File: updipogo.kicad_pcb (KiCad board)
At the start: 2 copper layers, 32 x 10.7 mm, 13 parts, among them J1 USB_C_Receptacle_USB2.0, J2 1.27, J3 2.54, J4 Header, U1 CH340N

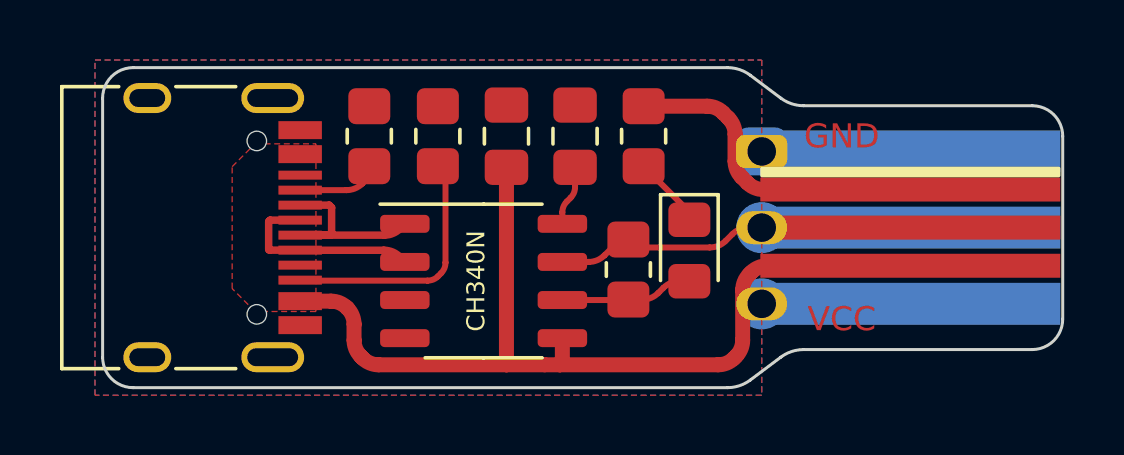
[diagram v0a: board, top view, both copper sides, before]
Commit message: update pcb for new pinout
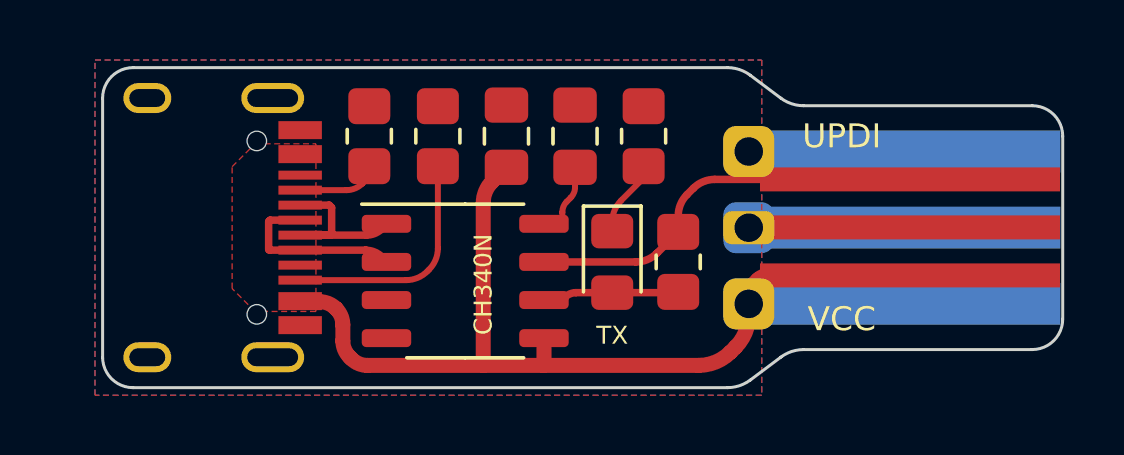
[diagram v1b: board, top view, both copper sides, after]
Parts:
- J2: value 1.27 -> 1.6mm; footprint local:PogoPins_1.27mm -> local:PogoPins_1.6mm
- J3: value 2.54 -> 2.54mm
- moved D1 2.60 mm to (125.7, 77.8)
- moved R3 1.68 mm to (127.9, 77.8)
- moved U1 0.61 mm to (120.8, 78.5)
- moved J4 0.43 mm to (130.2, 79.2)
- moved ahoi 0.28 mm to (120.2, 78.7)
- turned J2 to 90 degrees
- turned J3 to 90 degrees
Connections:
- J2 pad 1: GND -> VBUS
- J2 pad 2: /UPDI -> GND
- J2 pad 3: VBUS -> /RX
- J3 pad 1: GND -> VBUS
- J3 pad 2: /UPDI -> GND
- J3 pad 3: VBUS -> /RX
- J4 pad 1: GND -> VBUS
- J4 pad 2: /UPDI -> GND
- J4 pad 3: VBUS -> /RX
- R3 pad 2: /UPDI -> /RX
- U1 pad 7: /UPDI -> /RX
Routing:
- net /RX: track 0.00 -> 13.8 mm
- net /UPDI: track 12.1 -> 0.00 mm
- net GND: track 10.8 -> 0.00 mm
- net /USB_D-: track 6.67 -> 6.07 mm
- net /USB_D+: track 6.65 -> 6.05 mm

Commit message: reverse pin numbering and add footprint for pads
updi pin is now pin 1 and is square / boxed-in on programming pads
footprint
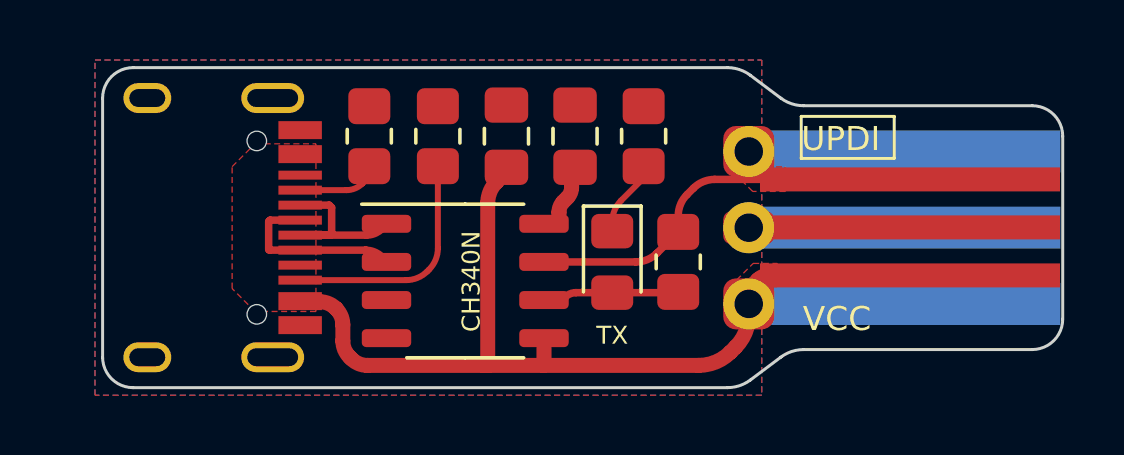
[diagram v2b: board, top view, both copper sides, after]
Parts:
- moved ahoi 0.22 mm to (120.1, 78.5)
- turned J2 to -90 degrees
- turned J3 to -90 degrees
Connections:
- J2 pad 1: VBUS -> /RX
- J2 pad 3: /RX -> VBUS
- J3 pad 1: VBUS -> /RX
- J3 pad 3: /RX -> VBUS
- J4 pad 1: VBUS -> /RX
- J4 pad 3: /RX -> VBUS
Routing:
- added copper zone on F.Cu, net /RX

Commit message: change milling radius on tip narrowing
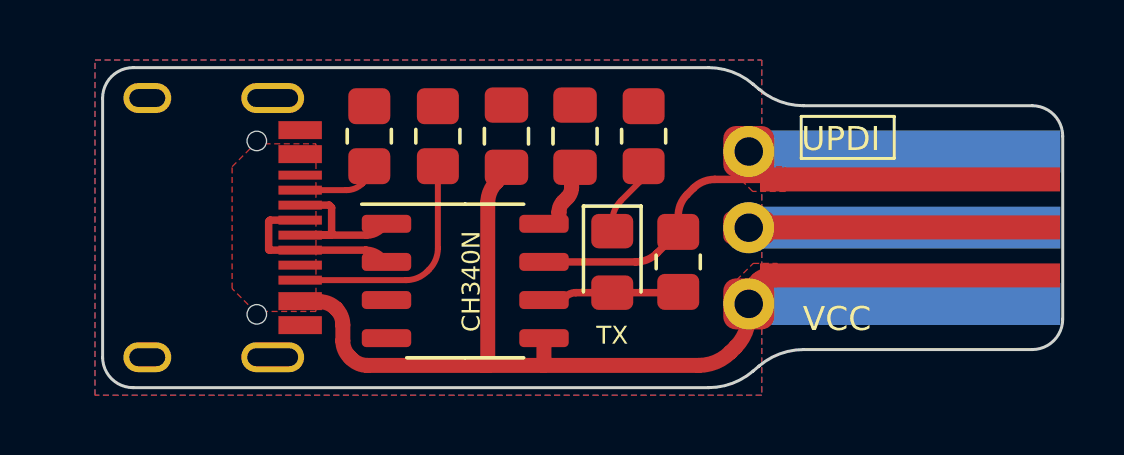
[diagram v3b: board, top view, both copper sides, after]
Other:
- outline, holes or cut-outs redrawn
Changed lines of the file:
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@@
   )
   (gr_rect (start 132 73) (end 135.1 74.4) (layer "F.SilkS") (width 0.1) (fill none))
-  (gr_line (start 130.302 81.788) (end 131.318 81.026) (layer "Edge.Cuts") (width 0.1))
+  (gr_arc (start 132.08 83.058) (end 132.08 80.772) (angle -40.60129465) (layer "Edge.Cuts") (width 0.1))
+  (gr_arc (start 128.905 79.756) (end 128.905 82.042) (angle -40.60129465) (layer "Edge.Cuts") (width 0.1))
   (gr_line (start 139.7 80.772) (end 132.08 80.772) (layer "Edge.Cuts") (width 0.1))
-  (gr_arc (start 129.54 80.772) (end 129.54 82.042) (angle -36.86989765) (layer "Edge.Cuts") (width 0.1))
-  (gr_line (start 129.54 82.042) (end 109.728 82.042) (layer "Edge.Cuts") (width 0.1))
-  (gr_arc (start 132.08 82.042) (end 132.08 80.772) (angle -36.86989765) (layer "Edge.Cuts") (width 0.1))
-  (gr_arc (start 132.08 71.374) (end 132.08 72.644) (angle 36.86989765) (layer "Edge.Cuts") (width 0.1))
-  (gr_line (start 109.728 71.374) (end 129.54 71.374) (layer "Edge.Cuts") (width 0.1))
+  (gr_line (start 128.905 82.042) (end 109.728 82.042) (layer "Edge.Cuts") (width 0.1))
+  (gr_arc (start 132.08 70.358) (end 132.08 72.644) (angle 40.60129465) (layer "Edge.Cuts") (width 0.1))
+  (gr_line (start 109.728 71.374) (end 128.905 71.374) (layer "Edge.Cuts") (width 0.1))
   (gr_arc (start 109.728 72.39) (end 109.728 71.374) (angle -90) (layer "Edge.Cuts") (width 0.1))
   (gr_line (start 108.712 81.026) (end 108.712 72.39) (layer "Edge.Cuts") (width 0.1))
@@
   (gr_line (start 140.716 73.66) (end 140.716 79.756) (layer "Edge.Cuts") (width 0.1))
   (gr_arc (start 139.7 79.756) (end 139.7 80.772) (angle -90) (layer "Edge.Cuts") (width 0.1))
-  (gr_line (start 131.318 72.39) (end 130.302 71.628) (layer "Edge.Cuts") (width 0.1))
   (gr_line (start 139.7 72.644) (end 132.08 72.644) (layer "Edge.Cuts") (width 0.1))
-  (gr_arc (start 129.54 72.644) (end 129.54 71.374) (angle 36.86989765) (layer "Edge.Cuts") (width 0.1))
+  (gr_line (start 130.392709 81.491661) (end 130.592291 81.322339) (layer "Edge.Cuts") (width 0.1))
+  (gr_arc (start 128.905 73.66) (end 128.905 71.374) (angle 40.60129465) (layer "Edge.Cuts") (width 0.1))
+  (gr_line (start 130.392709 71.924339) (end 130.592291 72.093661) (layer "Edge.Cuts") (width 0.1))
   (gr_text "UPDI" (at 129.159 74.168) (layer "B.SilkS")
     (effects (font (size 0.8 0.8) (thickness 0.2)) (justify left mirror))

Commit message: fix usb polarity
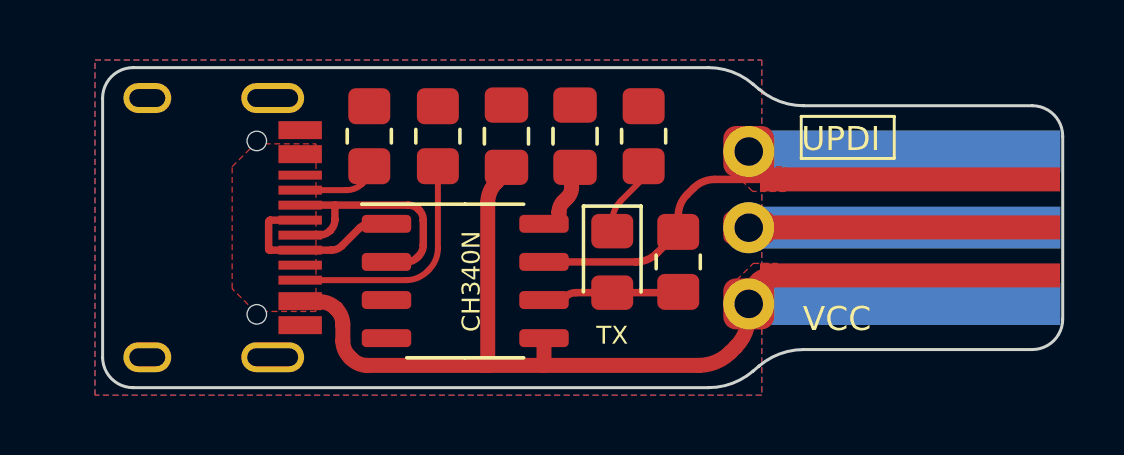
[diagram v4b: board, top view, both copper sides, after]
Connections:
- J1 pad A6: /USB_D- -> /USB_D+
- J1 pad A7: /USB_D+ -> /USB_D-
- J1 pad B6: /USB_D- -> /USB_D+
- J1 pad B7: /USB_D+ -> /USB_D-
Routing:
- net /USB_D-: track 6.07 -> 8.68 mm
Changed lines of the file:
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@@
       (net 11 "/CC1") (pinfunction "CC1") (pintype "bidirectional"))
     (pad "A6" smd rect (at -0.25 -4.045 270) (size 0.3 1.45) (layers "F.Cu" "F.Paste" "F.Mask")
-      (net 6 "/USB_D-") (pinfunction "D+") (pintype "bidirectional"))
+      (net 7 "/USB_D+") (pinfunction "D+") (pintype "bidirectional"))
     (pad "A7" smd rect (at 0.25 -4.045 270) (size 0.3 1.45) (layers "F.Cu" "F.Paste" "F.Mask")
-      (net 7 "/USB_D+") (pinfunction "D-") (pintype "bidirectional"))
+      (net 6 "/USB_D-") (pinfunction "D-") (pintype "bidirectional"))
     (pad "A8" smd rect (at 1.25 -4.045 270) (size 0.3 1.45) (layers "F.Cu" "F.Paste" "F.Mask")
       (net 3 "unconnected-(J1-PadA8)") (pinfunction "SBU1") (pintype "bidirectional+no_connect"))
@@
       (net 10 "/CC2") (pinfunction "CC2") (pintype "bidirectional"))
     (pad "B6" smd rect (at 0.75 -4.045 270) (size 0.3 1.45) (layers "F.Cu" "F.Paste" "F.Mask")
-      (net 6 "/USB_D-") (pinfunction "D+") (pintype "bidirectional"))
+      (net 7 "/USB_D+") (pinfunction "D+") (pintype "bidirectional"))
     (pad "B7" smd rect (at -0.75 -4.045 270) (size 0.3 1.45) (layers "F.Cu" "F.Paste" "F.Mask")
-      (net 7 "/USB_D+") (pinfunction "D-") (pintype "bidirectional"))
+      (net 6 "/USB_D-") (pinfunction "D-") (pintype "bidirectional"))
     (pad "B8" smd rect (at -1.75 -4.045 270) (size 0.3 1.45) (layers "F.Cu" "F.Paste" "F.Mask")
       (net 4 "unconnected-(J1-PadB8)") (pinfunction "SBU2") (pintype "bidirectional+no_connect"))
@@
     (fp_line (start -2.2 5.25) (end -2.2 -5.25) (layer "F.CrtYd") (width 0.05))
     (pad "1" smd rect (at -1.6 0 270) (size 0.8 10) (layers "F.Cu" "F.Mask")
-      (net 13 "/RX") (pinfunction "Pin_1"))
+      (net 13 "/RX") (pinfunction "Pin_1") (pintype "passive"))
     (pad "2" smd rect (at 0 0 270) (size 0.8 10) (layers "F.Cu" "F.Mask")
-      (net 1 "GND") (pinfunction "Pin_2"))
+      (net 1 "GND") (pinfunction "Pin_2") (pintype "passive"))
     (pad "3" smd rect (at 1.6 0 270) (size 0.8 10) (layers "F.Cu" "F.Mask")
-      (net 2 "VBUS") (pinfunction "Pin_3"))
+      (net 2 "VBUS") (pinfunction "Pin_3") (pintype "passive"))
   )
   (footprint "Resistor_SMD:R_0805_2012Metric_Pad1.20x1.40mm_HandSolder" (layer "F.Cu")
@@
     (fp_line (start -0.32 -2.22) (end -0.32 -2.86) (layer "B.Fab") (width 0.1))
     (pad "1" smd roundrect (at 0 -5.08) (size 1.7 1.7) (layers "F.Cu" "F.Mask") (roundrect_rratio 0.25)
-      (net 13 "/RX") (pinfunction "Pin_1"))
+      (net 13 "/RX") (pinfunction "Pin_1") (pintype "passive"))
     (pad "1" thru_hole circle (at 0 -5.08) (size 1.7 1.7) (drill 0.95) (layers *.Cu *.Mask)
-      (net 13 "/RX") (pinfunction "Pin_1") (zone_connect 2))
+      (net 13 "/RX") (pinfunction "Pin_1") (pintype "passive") (zone_connect 2))
     (pad "2" thru_hole circle (at 0 -2.54) (size 1.7 1.7) (drill 0.95) (layers *.Cu "B.Mask") (remove_unused_layers)
-      (net 1 "GND") (pinfunction "Pin_2") (zone_connect 2))
+      (net 1 "GND") (pinfunction "Pin_2") (pintype "passive") (zone_connect 2))
     (pad "2" smd roundrect (at 0 -2.54) (size 1.7 1.1) (layers "F.Cu" "F.Mask") (roundrect_rratio 0.25)
-      (net 1 "GND") (pinfunction "Pin_2"))
+      (net 1 "GND") (pinfunction "Pin_2") (pintype "passive"))
     (pad "2" smd circle (at 0 -2.54) (size 1.7 1.7) (layers "B.Cu" "B.Mask")
-      (net 1 "GND") (pinfunction "Pin_2"))
+      (net 1 "GND") (pinfunction "Pin_2") (pintype "passive"))
     (pad "3" smd roundrect (at 0 0) (size 1.7 1.7) (layers "F.Cu" "F.Mask") (roundrect_rratio 0.25)
-      (net 2 "VBUS") (pinfunction "Pin_3"))
+      (net 2 "VBUS") (pinfunction "Pin_3") (pintype "passive"))
     (pad "3" thru_hole circle (at 0 0) (size 1.7 1.7) (drill 0.95) (layers *.Cu *.Mask)
-      (net 2 "VBUS") (pinfunction "Pin_3") (zone_connect 2))
+      (net 2 "VBUS") (pinfunction "Pin_3") (pintype "passive") (zone_connect 2))
     (model "${KISYS3DMOD}/Connector_PinHeader_2.54mm.3dshapes/PinHeader_1x03_P2.54mm_Horizontal.wrl"
       (offset (xyz 0 0 0))
@@
   (arc (start 116.50033 79.41633) (mid 116.66291 79.659647) (end 116.72 79.94666) (width 0.5) (layer "F.Cu") (net 2))
   (arc (start 116.72 80.48134) (mid 116.77709 80.768353) (end 116.93967 81.01167) (width 0.5) (layer "F.Cu") (net 2))
-  (segment (start 114.272978 77.458) (end 114.247489 77.432511) (width 0.25) (layer "F.Cu") (net 6))
-  (segment (start 115.297 77.458) (end 114.272978 77.458) (width 0.25) (layer "F.Cu") (net 6))
-  (segment (start 117.487511 77.461511) (end 117.484 77.458) (width 0.25) (layer "F.Cu") (net 6))
-  (segment (start 114.247489 76.506511) (end 114.296 76.458) (width 0.25) (layer "F.Cu") (net 6))
-  (segment (start 114.247489 77.432511) (end 114.247489 76.506511) (width 0.25) (layer "F.Cu") (net 6))
-  (segment (start 114.296 76.458) (end 115.297 76.458) (width 0.25) (layer "F.Cu") (net 6))
-  (segment (start 115.297 77.458) (end 117.484 77.458) (width 0.25) (layer "F.Cu") (net 6))
-  (segment (start 118.017841 77.681181) (end 118.18766 77.851) (width 0.25) (layer "F.Cu") (net 6))
-  (arc (start 118.017841 77.681181) (mid 117.774524 77.518601) (end 117.487511 77.461511) (width 0.25) (layer "F.Cu") (net 6))
-  (segment (start 115.297 75.958) (end 116.264689 75.958) (width 0.25) (layer "F.Cu") (net 7))
-  (segment (start 116.346511 76.039822) (end 116.346511 76.932511) (width 0.25) (layer "F.Cu") (net 7))
-  (segment (start 118.03033 76.73833) (end 118.18766 76.581) (width 0.25) (layer "F.Cu") (net 7))
-  (segment (start 117.5 76.958) (end 115.297 76.958) (width 0.25) (layer "F.Cu") (net 7))
-  (segment (start 116.346511 76.932511) (end 116.321022 76.958) (width 0.25) (layer "F.Cu") (net 7))
-  (segment (start 116.264689 75.958) (end 116.346511 76.039822) (width 0.25) (layer "F.Cu") (net 7))
-  (segment (start 116.321022 76.958) (end 115.297 76.958) (width 0.25) (layer "F.Cu") (net 7))
-  (arc (start 118.03033 76.73833) (mid 117.787013 76.90091) (end 117.5 76.958) (width 0.25) (layer "F.Cu") (net 7))
+  (segment (start 116.45648 76.436413) (end 116.45648 75.95648) (width 0.25) (layer "F.Cu") (net 6))
+  (segment (start 116.288447 76.811553) (end 116.310034 76.789966) (width 0.25) (layer "F.Cu") (net 6))
+  (segment (start 118.841893 77.851) (end 118.175 77.851) (width 0.25) (layer "F.Cu") (net 6))
+  (segment (start 116.45648 75.95648) (end 118.896487 75.95648) (width 0.25) (layer "F.Cu") (net 6))
+  (segment (start 115.297 76.958) (end 115.934893 76.958) (width 0.25) (layer "F.Cu") (net 6))
+  (segment (start 119.4 76.459993) (end 119.4 77.292893) (width 0.25) (layer "F.Cu") (net 6))
+  (segment (start 115.29852 75.95648) (end 116.45648 75.95648) (width 0.25) (layer "F.Cu") (net 6))
+  (segment (start 119.250041 76.102927) (end 119.253554 76.10644) (width 0.25) (layer "F.Cu") (net 6))
+  (segment (start 119.253553 77.646447) (end 119.195446 77.704554) (width 0.25) (layer "F.Cu") (net 6))
+  (segment (start 115.297 75.958) (end 115.29852 75.95648) (width 0.25) (layer "F.Cu") (net 6))
+  (arc (start 119.253553 77.646447) (mid 119.36194 77.484235) (end 119.4 77.292893) (width 0.25) (layer "F.Cu") (net 6))
+  (arc (start 119.195446 77.704554) (mid 119.033234 77.81294) (end 118.841893 77.851) (width 0.25) (layer "F.Cu") (net 6))
+  (arc (start 116.45648 76.436413) (mid 116.41842 76.627754) (end 116.310034 76.789966) (width 0.25) (layer "F.Cu") (net 6))
+  (arc (start 116.288447 76.811553) (mid 116.126235 76.91994) (end 115.934893 76.958) (width 0.25) (layer "F.Cu") (net 6))
+  (arc (start 119.250041 76.102927) (mid 119.087829 75.99454) (end 118.896487 75.95648) (width 0.25) (layer "F.Cu") (net 6))
+  (arc (start 119.253554 76.10644) (mid 119.36194 76.268652) (end 119.4 76.459993) (width 0.25) (layer "F.Cu") (net 6))
+  (segment (start 114.272978 77.458) (end 114.247489 77.432511) (width 0.25) (layer "F.Cu") (net 7))
+  (segment (start 117.626107 76.581) (end 118.175 76.581) (width 0.25) (layer "F.Cu") (net 7))
+  (segment (start 115.297 77.458) (end 116.334893 77.458) (width 0.25) (layer "F.Cu") (net 7))
+  (segment (start 115.297 77.458) (end 114.272978 77.458) (width 0.25) (layer "F.Cu") (net 7))
+  (segment (start 114.247489 76.506511) (end 114.296 76.458) (width 0.25) (layer "F.Cu") (net 7))
+  (segment (start 116.688447 77.311553) (end 117.272554 76.727446) (width 0.25) (layer "F.Cu") (net 7))
+  (segment (start 114.247489 77.432511) (end 114.247489 76.506511) (width 0.25) (layer "F.Cu") (net 7))
+  (segment (start 114.296 76.458) (end 115.297 76.458) (width 0.25) (layer "F.Cu") (net 7))
+  (arc (start 116.334893 77.458) (mid 116.526235 77.41994) (end 116.688447 77.311553) (width 0.25) (layer "F.Cu") (net 7))
+  (arc (start 117.272554 76.727446) (mid 117.434766 76.61906) (end 117.626107 76.581) (width 0.25) (layer "F.Cu") (net 7))
   (segment (start 124.069893 75.841553) (end 124.2 75.711446) (width 0.5) (layer "F.Cu") (net 8))
   (segment (start 123.923446 76.581) (end 123.923446 76.195107) (width 0.5) (layer "F.Cu") (net 8))

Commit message: add note about lit-up LED
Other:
- board text added: "TODO: LED does {dblquote}nothing{dblquote} because it's constantly lit up"
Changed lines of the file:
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@@
     (effects (font (size 1 1) (thickness 0.15)) (justify left mirror))
+  )
+  (gr_text "TODO: LED does {dblquote}nothing{dblquote} because\nit's constantly lit up" (at 129 67.6) (layer "F.Fab")
+    (effects (font (size 1 1) (thickness 0.2)))
   )
   (segment (start 130.396447 78.603553) (end 130.553554 78.446446) (width 0.5) (layer "F.Cu") (net 2))

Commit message: connect led to RTS and update pcb layout a bit
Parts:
- removed ahoi: 2021, local:ahoi
- added kibuzzard-630501DC: G***, kibuzzard-630501DC, B.Cu at (119.1, 75.9)
- added kibuzzard-6305024E: G***, kibuzzard-6305024E, F.Cu at (133.7, 73.4)
- added kibuzzard-6305027C: G***, kibuzzard-6305027C, F.Cu at (132.8, 80.0)
- moved C2 7.57 mm to (128.0, 78.5)
- moved R4 4.57 mm to (122.2, 73.7)
- moved D1 4.37 mm to (124.5, 73.7)
- moved C1 2.29 mm to (126.7, 73.7)
- moved R3 2.25 mm to (125.8, 78.5)
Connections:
- D1 pad 1: Net-(D1-Pad1) -> Net-(R4-Pad1)
- D1 pad 2: /TX -> VBUS
- R4 pad 1: GND -> Net-(R4-Pad1)
- R4 pad 2: Net-(D1-Pad1) -> Net-(U1-Pad4)
- U1 pad 4: unconnected-(U1-Pad4) -> Net-(U1-Pad4)
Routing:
- net Net-(U1-Pad4): track 0.00 -> 8.92 mm
- net /RX: track 13.8 -> 8.23 mm
- net VBUS: track 31.8 -> 34.8 mm
- net Net-(D1-Pad1): track 2.55 -> 0.00 mm
- net Net-(R4-Pad1): track 0.00 -> 2.30 mm
- net /V3: track 2.01 -> 4.01 mm
- net /TX: track 4.55 -> 2.59 mm
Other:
- outline, holes or cut-outs redrawn
- board text added: "2022 ansemjo"
- board text added: "5V"
- board text removed: "TODO: LED does {dblquote}nothing{dblquote} because it's constantly lit up"
- board text removed: "TX"
- board text removed: "VCC"
- board text removed: "updipogo_v1"
